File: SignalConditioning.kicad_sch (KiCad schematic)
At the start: 51 parts, among them J21 Screw_Terminal_01x03, J22 Screw_Terminal_01x02

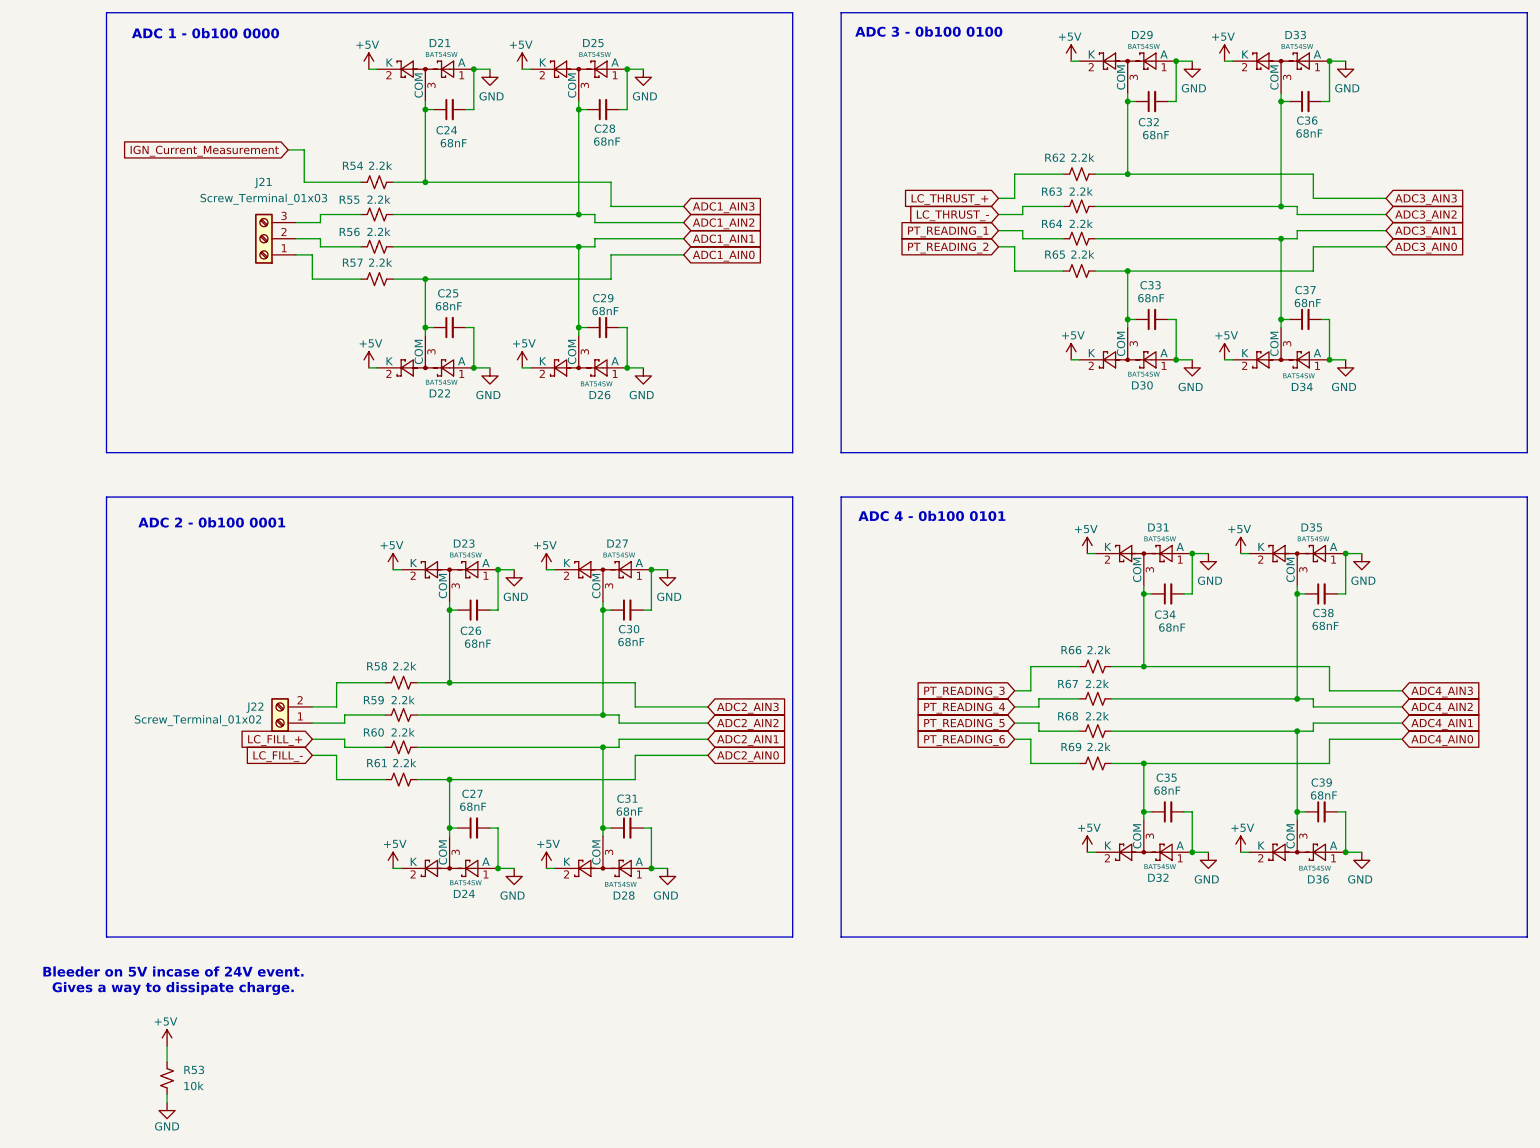
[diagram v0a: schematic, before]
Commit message: revamped schematic to be more readable
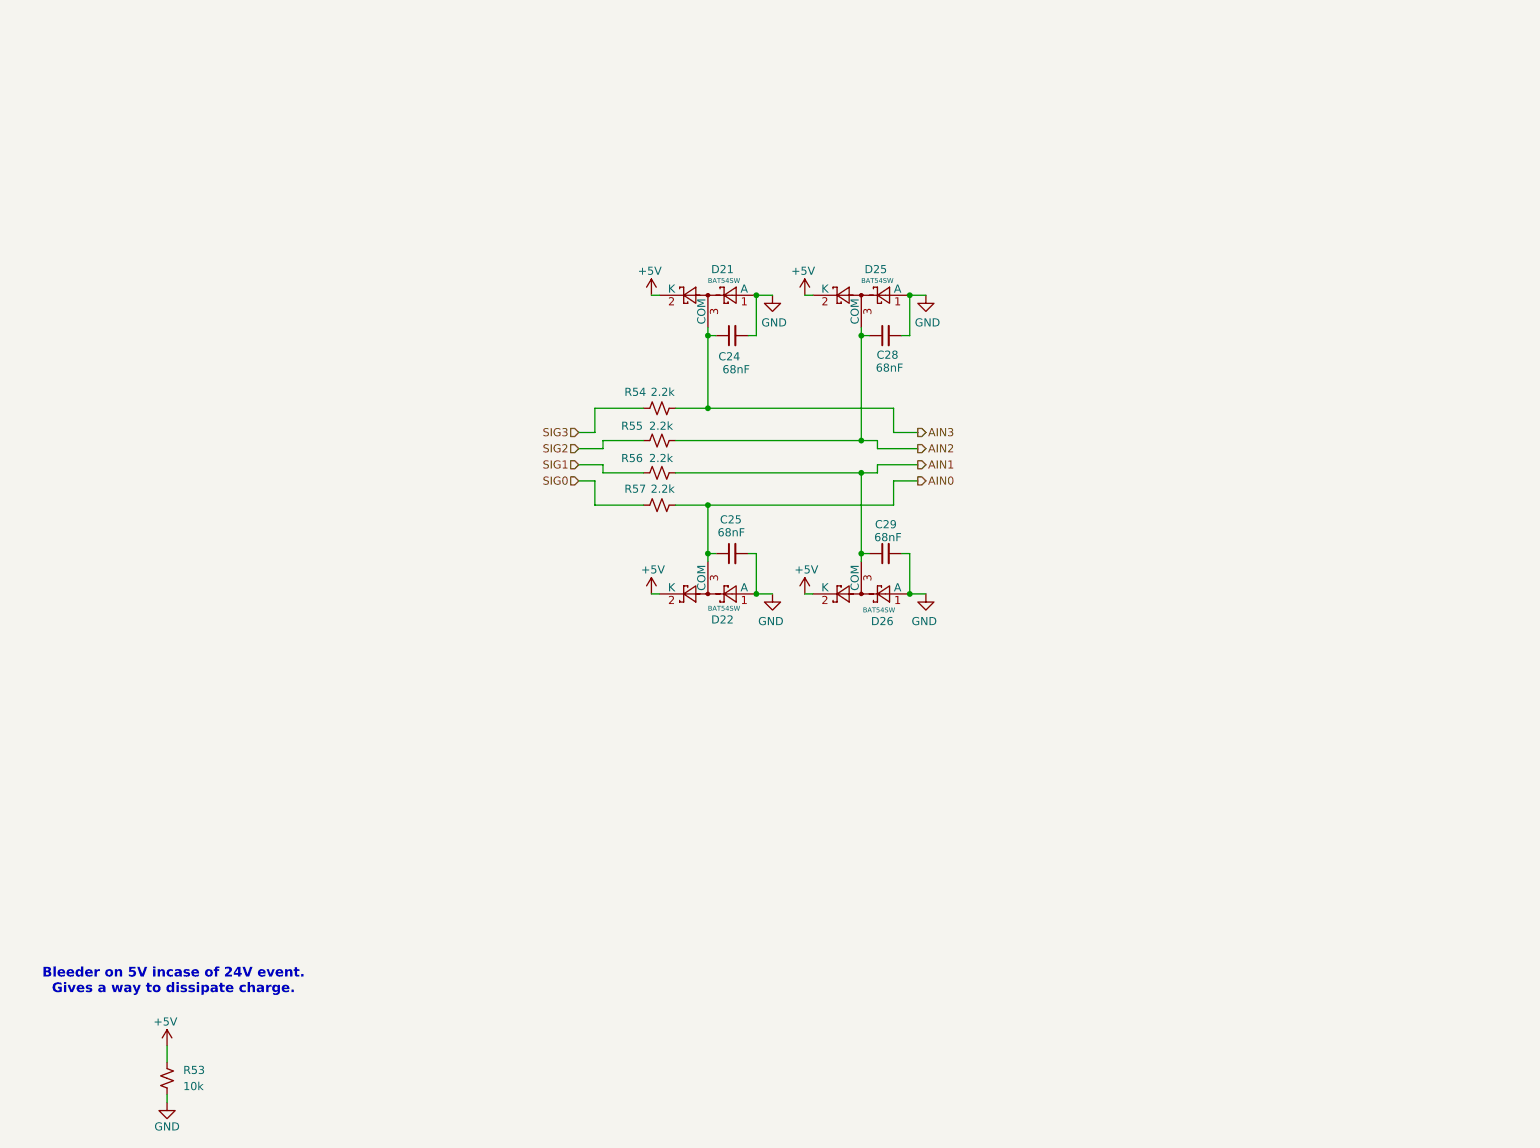
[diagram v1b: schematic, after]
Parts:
- removed C26, C27, C30, C31, C32, C33, C34, C35, C36, C37, C38, C39: 68nF, Capacitor_SMD:C_0805_2012Metric, symbol Device:C_Small
- removed D23, D24, D27, D28, D29, D30, D31, D32, D33, D34, D35, D36: BAT54SW, Package_TO_SOT_SMD:SOT-323_SC-70, symbol Diode:BAT54SW
- removed J21: Screw_Terminal_01x03, TerminalBlock:TerminalBlock_Xinya_XY308-2.54-3P_1x03_P2.54mm_Horizontal, symbol Connector:Screw_Terminal_01x03
- removed J22: Screw_Terminal_01x02, TerminalBlock:TerminalBlock_Xinya_XY308-2.54-2P_1x02_P2.54mm_Horizontal, symbol Connector:Screw_Terminal_01x02
- removed R58, R59, R60, R61, R62, R63, R64, R65, R66, R67, R68, R69: 2.2k, Resistor_SMD:R_0402_1005Metric, symbol Device:R_Small_US
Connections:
- net SIG1: now reaches R56.1
- net SIG2: now reaches R55.1
- net SIG0: now reaches R57.1
- net ADC1_AIN0 renamed AIN0
- net ADC1_AIN1 renamed AIN1
- net ADC1_AIN2 renamed AIN2
- net ADC1_AIN3 renamed AIN3
- net IGN_Current_Measurement renamed SIG3
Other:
- note removed: "ADC 1 - 0b100 0000"
- note removed: "ADC 2 - 0b100 0001"
- note removed: "ADC 3 - 0b100 0100"
- note removed: "ADC 4 - 0b100 0101"
- moved on the sheet: C24, C25, C28, C29, D21, D22, D25, D26, R54, R55, R56, R57
